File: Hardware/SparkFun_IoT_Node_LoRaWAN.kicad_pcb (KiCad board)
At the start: 4 copper layers, 59 x 82 mm, 234 parts, among them J1 USB_C_Receptacle, J10 microSD_Friction, J11 Qwiic_RA, J2 Conn_01x03, J3 USB_C_Receptacle, J4 SWD, J5 Conn_01x10, J6 Conn_01x10, J7 Conn_01x10, J8 Conn_01x10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

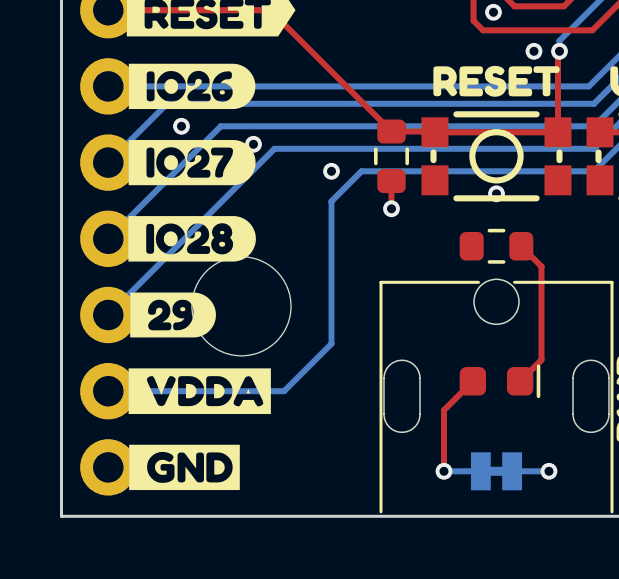
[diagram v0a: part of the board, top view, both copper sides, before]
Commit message: Cosmetic tweaks
Nudge IO 29 silk away from mounting hole
Add VDDA RC filter cutoff frequency
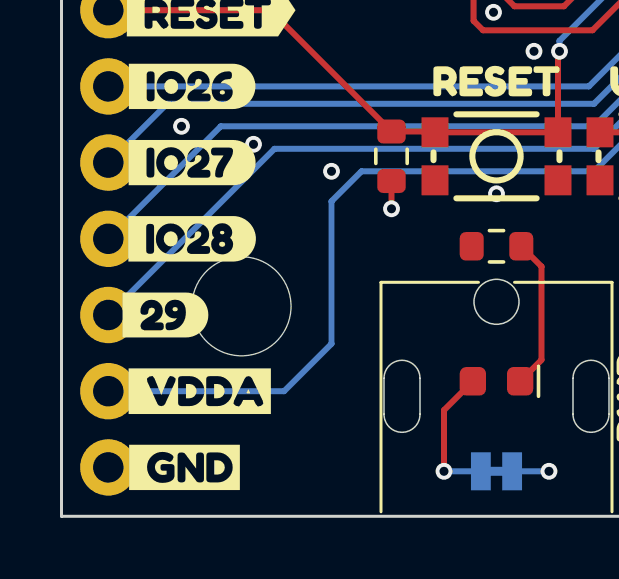
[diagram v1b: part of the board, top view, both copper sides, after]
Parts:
- moved kibuzzard-669EA5FC 0.25 mm to (74.0, 134.3)
- moved kibuzzard-669EA604 0.25 mm to (74.0, 134.3)
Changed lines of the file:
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@@
 	(footprint "kibuzzard-669EA604"
 		(layer "F.Cu")
-		(at 74.219 134.29)
+		(at 73.965 134.29)
 		(descr "Generated with KiBuzzard")
 		(tags "kb_params=eyJBbGlnbm1lbnRDaG9pY2UiOiAiQ2VudGVyIiwgIkNhcExlZnRDaG9pY2UiOiAiWyIsICJDYXBSaWdodENob2ljZSI6ICIpIiwgIkZvbnRDb21ib0JveCI6ICJGcmVkZHlTcGFyay1SZWd1bGFyIiwgIkhlaWdodEN0cmwiOiAxLjAsICJMYXllckNvbWJvQm94IjogIkYuU2lsa1MiLCAiTGluZVNwYWNpbmdDdHJsIjogMS41LCAiTXVsdGlMaW5lVGV4dCI6ICIyOSIsICJQYWRkaW5nQm90dG9tQ3RybCI6IDIuMCwgIlBhZGRpbmdMZWZ0Q3RybCI6IDUuMCwgIlBhZGRpbmdSaWdodEN0cmwiOiAwLjAsICJQYWRkaW5nVG9wQ3RybCI6IDIuMCwgIldpZHRoQ3RybCI6IDAuMCwgImFkdmFuY2VkQ2hlY2tib3giOiBmYWxzZSwgImlubGluZUZvcm1hdFRleHRib3giOiBmYWxzZSwgImxpbmVvdmVyU3R5bGVDaG9pY2UiOiAiU3F1YXJlIiwgImxpbmVvdmVyVGhpY2tuZXNzQ3RybCI6IDF9")
@@
 	(footprint "kibuzzard-669EA5FC"
 		(layer "B.Cu")
-		(at 74.219 134.29 180)
+		(at 73.965 134.29 180)
 		(descr "Generated with KiBuzzard")
 		(tags "kb_params=eyJBbGlnbm1lbnRDaG9pY2UiOiAiQ2VudGVyIiwgIkNhcExlZnRDaG9pY2UiOiAiKCIsICJDYXBSaWdodENob2ljZSI6ICJdIiwgIkZvbnRDb21ib0JveCI6ICJGcmVkZHlTcGFyay1SZWd1bGFyIiwgIkhlaWdodEN0cmwiOiAxLjAsICJMYXllckNvbWJvQm94IjogIkYuU2lsa1MiLCAiTGluZVNwYWNpbmdDdHJsIjogMS41LCAiTXVsdGlMaW5lVGV4dCI6ICIyOSIsICJQYWRkaW5nQm90dG9tQ3RybCI6IDIuMCwgIlBhZGRpbmdMZWZ0Q3RybCI6IDAuMCwgIlBhZGRpbmdSaWdodEN0cmwiOiA1LjAsICJQYWRkaW5nVG9wQ3RybCI6IDIuMCwgIldpZHRoQ3RybCI6IDAuMCwgImFkdmFuY2VkQ2hlY2tib3giOiBmYWxzZSwgImlubGluZUZvcm1hdFRleHRib3giOiBmYWxzZSwgImxpbmVvdmVyU3R5bGVDaG9pY2UiOiAiU3F1YXJlIiwgImxpbmVvdmVyVGhpY2tuZXNzQ3RybCI6IDF9")

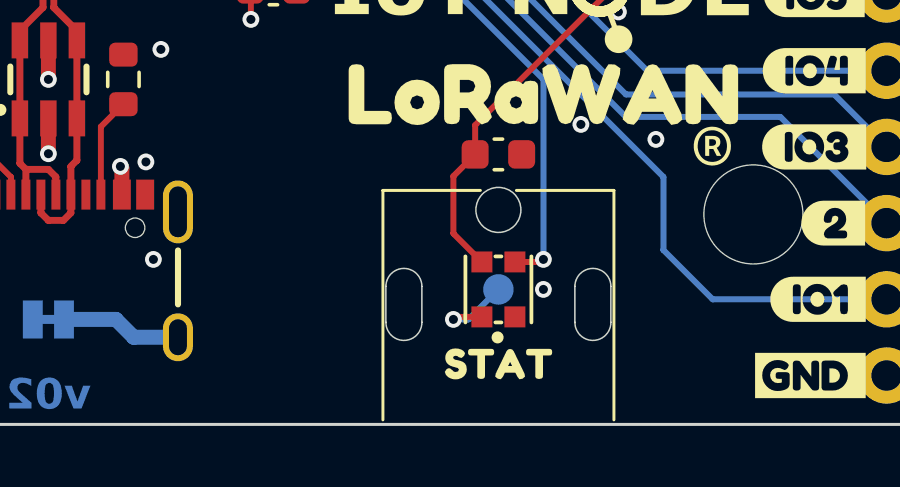
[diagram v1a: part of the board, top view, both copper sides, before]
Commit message: Move STAT silk
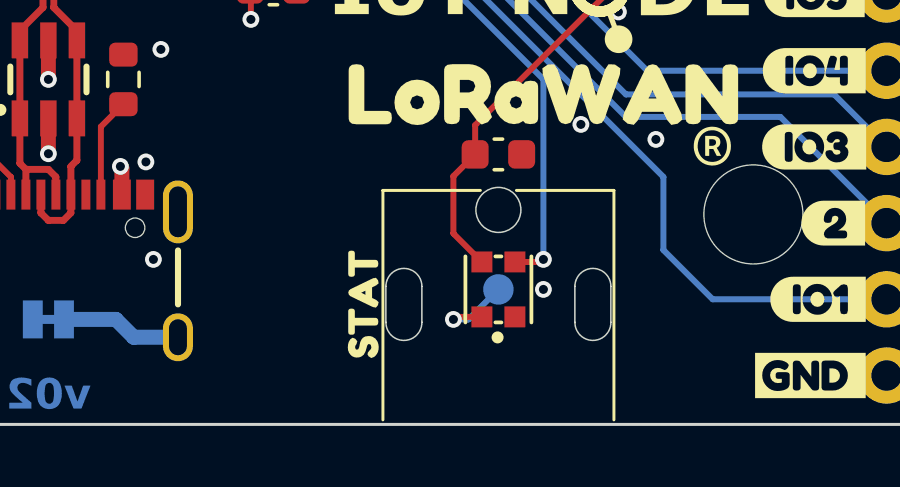
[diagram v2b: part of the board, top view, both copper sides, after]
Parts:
- moved kibuzzard-66999523 4.92 mm to (110.5, 137.0), turned to 90 degrees
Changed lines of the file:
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@@
 	(footprint "kibuzzard-66999523"
 		(layer "F.Cu")
-		(at 115 138.9875)
+		(at 110.5 137 90)
 		(descr "Generated with KiBuzzard")
 		(tags "kb_params=eyJBbGlnbm1lbnRDaG9pY2UiOiAiQ2VudGVyIiwgIkNhcExlZnRDaG9pY2UiOiAiIiwgIkNhcFJpZ2h0Q2hvaWNlIjogIiIsICJGb250Q29tYm9Cb3giOiAiRnJlZGR5U3BhcmstUmVndWxhciIsICJIZWlnaHRDdHJsIjogMS4wLCAiTGF5ZXJDb21ib0JveCI6ICJGLlNpbGtTIiwgIkxpbmVTcGFjaW5nQ3RybCI6IDEuNSwgIk11bHRpTGluZVRleHQiOiAiU1RBVCIsICJQYWRkaW5nQm90dG9tQ3RybCI6IDIuMCwgIlBhZGRpbmdMZWZ0Q3RybCI6IDAuMCwgIlBhZGRpbmdSaWdodEN0cmwiOiAwLjAsICJQYWRkaW5nVG9wQ3RybCI6IDIuMCwgIldpZHRoQ3RybCI6IDAuMCwgImFkdmFuY2VkQ2hlY2tib3giOiBmYWxzZSwgImlubGluZUZvcm1hdFRleHRib3giOiBmYWxzZSwgImxpbmVvdmVyU3R5bGVDaG9pY2UiOiAiU3F1YXJlIiwgImxpbmVvdmVyVGhpY2tuZXNzQ3RybCI6IDF9")
 		(property "Reference" "kibuzzard-66999523"
-			(at 0 -3.568029 0)
+			(at 0 -3.568029 90)
 			(layer "F.SilkS")
 			(hide yes)
@@
 		)
 		(property "Value" "G***"
-			(at 0 3.568029 0)
+			(at 0 3.568029 90)
 			(layer "F.SilkS")
 			(hide yes)
@@
 		)
 		(property "Footprint" ""
-			(at 0 0 0)
+			(at 0 0 90)
 			(layer "F.Fab")
 			(hide yes)
@@
 		)
 		(property "Datasheet" ""
-			(at 0 0 0)
+			(at 0 0 90)
 			(layer "F.Fab")
 			(hide yes)
@@
 		)
 		(property "Description" ""
-			(at 0 0 0)
+			(at 0 0 90)
 			(layer "F.Fab")
 			(hide yes)
@@
 		(fp_poly
 			(pts
+				(xy 1.684549 -0.505722) (xy 1.725322 -0.503577) (xy 1.757511 -0.492132) (xy 1.784692 -0.458512)
+				(xy 1.793276 -0.395565) (xy 1.784692 -0.332618) (xy 1.756795 -0.298999) (xy 1.723891 -0.287554)
+				(xy 1.683119 -0.285408) (xy 1.485694 -0.285408) (xy 1.485694 0.369814) (xy 1.483548 0.41774) (xy 1.469957 0.455651)
+				(xy 1.4299 0.487124) (xy 1.355508 0.497139) (xy 1.281831 0.487124) (xy 1.243205 0.454936) (xy 1.230329 0.416309)
+				(xy 1.228183 0.368383) (xy 1.228183 -0.285408) (xy 1.029328 -0.285408) (xy 0.988555 -0.287554) (xy 0.956366 -0.298999)
+				(xy 0.929185 -0.332618) (xy 0.920601 -0.396996) (xy 0.929185 -0.459227) (xy 0.957082 -0.492132)
+				(xy 0.989986 -0.503577) (xy 1.030758 -0.505722) (xy 1.684549 -0.505722)
+			)
+			(stroke
+				(width 0)
+				(type solid)
+			)
+			(fill solid)
+			(layer "F.SilkS")
+		)
+		(fp_poly
+			(pts
 				(xy -0.248212 -0.505722) (xy -0.207439 -0.503577) (xy -0.17525 -0.492132) (xy -0.148069 -0.458512)
 				(xy -0.139485 -0.395565) (xy -0.148069 -0.332618) (xy -0.175966 -0.298999) (xy -0.20887 -0.287554)
@@
 			)
 			(stroke
-				(width 0)
-				(type solid)
-			)
-			(fill solid)
-			(layer "F.SilkS")
-		)
-		(fp_poly
-			(pts
-				(xy 1.684549 -0.505722) (xy 1.725322 -0.503577) (xy 1.757511 -0.492132) (xy 1.784692 -0.458512)
-				(xy 1.793276 -0.395565) (xy 1.784692 -0.332618) (xy 1.756795 -0.298999) (xy 1.723891 -0.287554)
-				(xy 1.683119 -0.285408) (xy 1.485694 -0.285408) (xy 1.485694 0.369814) (xy 1.483548 0.41774) (xy 1.469957 0.455651)
-				(xy 1.4299 0.487124) (xy 1.355508 0.497139) (xy 1.281831 0.487124) (xy 1.243205 0.454936) (xy 1.230329 0.416309)
-				(xy 1.228183 0.368383) (xy 1.228183 -0.285408) (xy 1.029328 -0.285408) (xy 0.988555 -0.287554) (xy 0.956366 -0.298999)
-				(xy 0.929185 -0.332618) (xy 0.920601 -0.396996) (xy 0.929185 -0.459227) (xy 0.957082 -0.492132)
-				(xy 0.989986 -0.503577) (xy 1.030758 -0.505722) (xy 1.684549 -0.505722)
-			)
-			(stroke

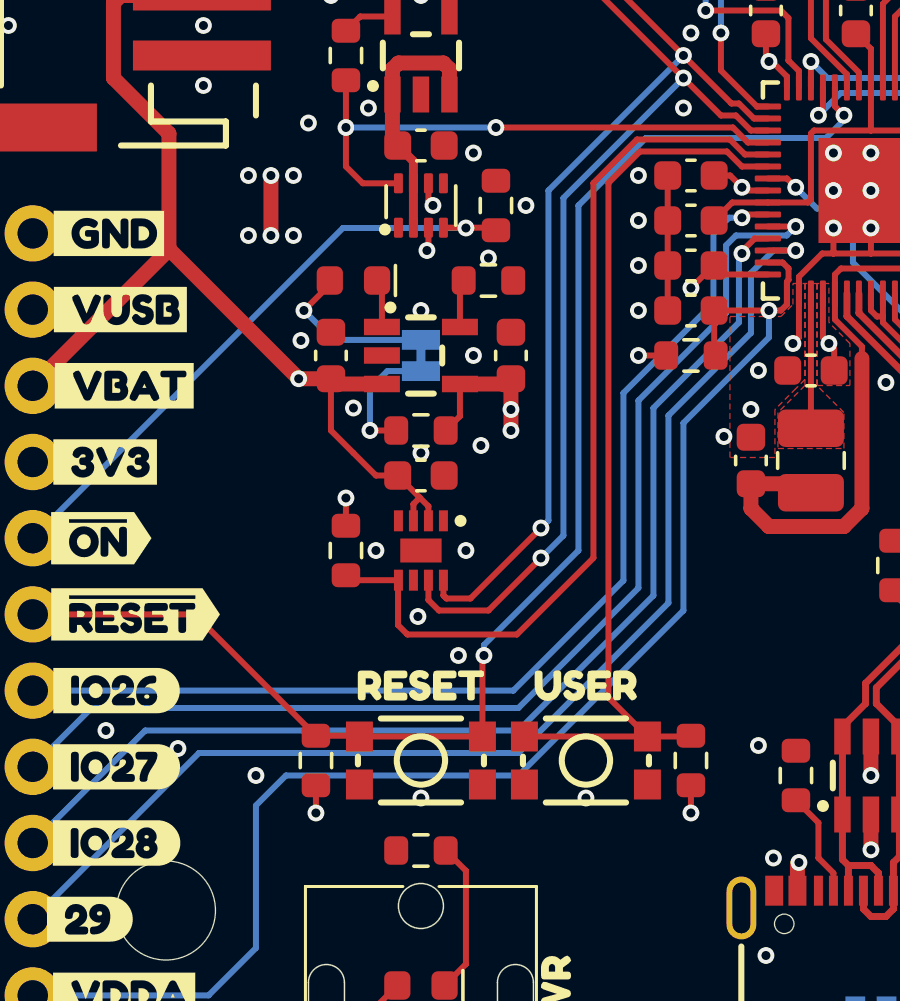
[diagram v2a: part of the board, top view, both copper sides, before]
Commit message: Spread out reset and user buttons
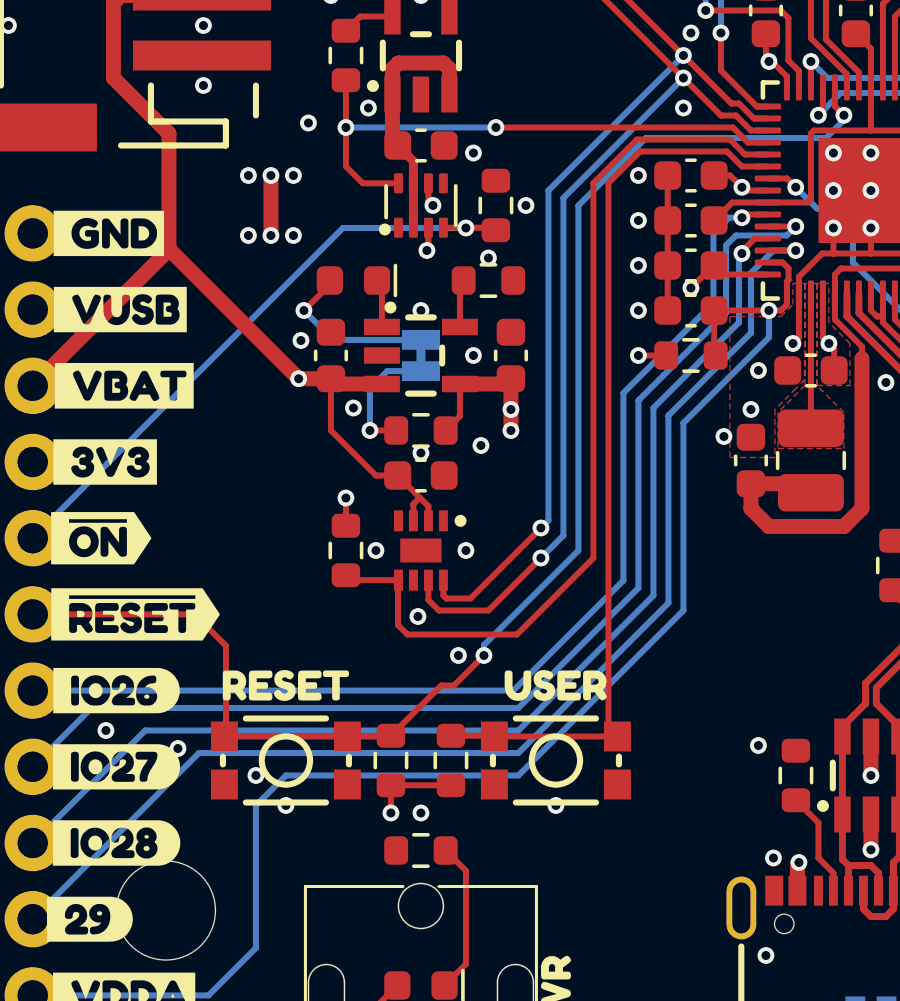
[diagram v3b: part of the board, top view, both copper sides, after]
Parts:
- moved R22 8.00 mm to (86.0, 129.0)
- moved SW3 4.50 mm to (80.5, 129.0)
- moved kibuzzard-6691B8DD 4.50 mm to (80.5, 126.5)
- moved R25 2.50 mm to (84.0, 129.0)
- moved SW2 1.00 mm to (89.5, 129.0)
- moved kibuzzard-669A9B0A 1.00 mm to (89.5, 126.5)
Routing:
- net 3.3V: track 59.5 -> 60.5 mm, vias 24 -> 23
- net GND: vias 167 -> 168
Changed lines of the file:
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@@
 	(footprint "SparkFun-Switch:Push_SMD_4.6x2.8mm"
 		(layer "F.Cu")
-		(at 90.5 129 180)
+		(at 89.5 129 180)
 		(tags "SparkFun Momentary Switch (Pushbutton)")
 		(property "Reference" "SW2"
@@
 	(footprint "SparkFun-Resistor:R_0603_1608Metric"
 		(layer "F.Cu")
-		(at 94 129 90)
+		(at 86 129 90)
 		(descr "Resistor SMD 0603 (1608 Metric), square (rectangular) end terminal, IPC_7351 nominal, (Body size source: IPC-SM-782 page 72, https://www.pcb-3d.com/wordpress/wp-content/uploads/ipc-sm-782a_amendment_1_and_2.pdf), generated with kicad-footprint-generator")
 		(tags "SparkFun resistor")
@@
 	(footprint "SparkFun-Switch:Push_SMD_4.6x2.8mm"
 		(layer "F.Cu")
-		(at 85 129 180)
+		(at 80.5 129 180)
 		(tags "SparkFun Momentary Switch (Pushbutton)")
 		(property "Reference" "SW3"
@@
 	(footprint "kibuzzard-6691B8DD"
 		(layer "F.Cu")
-		(at 85 126.5)
+		(at 80.5 126.5)
 		(descr "Generated with KiBuzzard")
 		(tags "kb_params=eyJBbGlnbm1lbnRDaG9pY2UiOiAiQ2VudGVyIiwgIkNhcExlZnRDaG9pY2UiOiAiIiwgIkNhcFJpZ2h0Q2hvaWNlIjogIiIsICJGb250Q29tYm9Cb3giOiAiRnJlZGR5U3BhcmstUmVndWxhciIsICJIZWlnaHRDdHJsIjogMS4wLCAiTGF5ZXJDb21ib0JveCI6ICJGLlNpbGtTIiwgIkxpbmVTcGFjaW5nQ3RybCI6IDEuNSwgIk11bHRpTGluZVRleHQiOiAiUkVTRVQiLCAiUGFkZGluZ0JvdHRvbUN0cmwiOiAyLjAsICJQYWRkaW5nTGVmdEN0cmwiOiAwLjAsICJQYWRkaW5nUmlnaHRDdHJsIjogMC4wLCAiUGFkZGluZ1RvcEN0cmwiOiAyLjAsICJXaWR0aEN0cmwiOiAwLjAsICJhZHZhbmNlZENoZWNrYm94IjogZmFsc2UsICJpbmxpbmVGb3JtYXRUZXh0Ym94IjogZmFsc2UsICJsaW5lb3ZlclN0eWxlQ2hvaWNlIjogIlNxdWFyZSIsICJsaW5lb3ZlclRoaWNrbmVzc0N0cmwiOiAxfQ==")
@@
 	(footprint "kibuzzard-669A9B0A"
 		(layer "F.Cu")
-		(at 90.5 126.5)
+		(at 89.5 126.5)
 		(descr "Generated with KiBuzzard")
 		(tags "kb_params=eyJBbGlnbm1lbnRDaG9pY2UiOiAiQ2VudGVyIiwgIkNhcExlZnRDaG9pY2UiOiAiIiwgIkNhcFJpZ2h0Q2hvaWNlIjogIiIsICJGb250Q29tYm9Cb3giOiAiRnJlZGR5U3BhcmstUmVndWxhciIsICJIZWlnaHRDdHJsIjogMS4wLCAiTGF5ZXJDb21ib0JveCI6ICJGLlNpbGtTIiwgIkxpbmVTcGFjaW5nQ3RybCI6IDEuNSwgIk11bHRpTGluZVRleHQiOiAiVVNFUiIsICJQYWRkaW5nQm90dG9tQ3RybCI6IDIuMCwgIlBhZGRpbmdMZWZ0Q3RybCI6IDAuMCwgIlBhZGRpbmdSaWdodEN0cmwiOiAwLjAsICJQYWRkaW5nVG9wQ3RybCI6IDIuMCwgIldpZHRoQ3RybCI6IDAuMCwgImFkdmFuY2VkQ2hlY2tib3giOiBmYWxzZSwgImlubGluZUZvcm1hdFRleHRib3giOiBmYWxzZSwgImxpbmVvdmVyU3R5bGVDaG9pY2UiOiAiU3F1YXJlIiwgImxpbmVvdmVyVGhpY2tuZXNzQ3RybCI6IDF9")
@@
 	(footprint "SparkFun-Resistor:R_0603_1608Metric"
 		(layer "F.Cu")
-		(at 81.5 129 90)
+		(at 84 129 90)
 		(descr "Resistor SMD 0603 (1608 Metric), square (rectangular) end terminal, IPC_7351 nominal, (Body size source: IPC-SM-782 page 72, https://www.pcb-3d.com/wordpress/wp-content/uploads/ipc-sm-782a_amendment_1_and_2.pdf), generated with kicad-footprint-generator")
 		(tags "SparkFun resistor")
@@
 		(layer "Dwgs.User")
 		(pts
-			(xy 85 129) (xy 100 129)
-		)
-		(height 21)
-		(gr_text "15 mm"
-			(at 92.5 148.85 0)
-			(layer "Dwgs.User")
-			(effects
-				(font
-					(size 1 1)
-					(thickness 0.15)
-				)
-			)
-		)
-		(format
-			(prefix "")
-			(suffix "")
-			(units 3)
-			(units_format 1)
-			(precision 4) suppress_zeroes)
-		(style
-			(thickness 0.15)
-			(arrow_length 1.27)
-			(text_position_mode 0)
-			(extension_height 0.58642)
-			(extension_offset 0.5) keep_text_aligned)
-	)
-	(dimension
-		(type aligned)
-		(layer "Dwgs.User")
-		(pts
 			(xy 58.5 81) (xy 141.5 81)
 		)
@@
 		(layer "Dwgs.User")
 		(pts
+			(xy 80.5 129) (xy 100 129)
+		)
+		(height 21)
+		(gr_text "19.5 mm"
+			(at 90.25 148.85 0)
+			(layer "Dwgs.User")
+			(effects
+				(font
+					(size 1 1)
+					(thickness 0.15)
+				)
+			)
+		)
+		(format
+			(prefix "")
+			(suffix "")
+			(units 3)
+			(units_format 1)
+			(precision 4) suppress_zeroes)
+		(style
+			(thickness 0.15)
+			(arrow_length 1.27)
+			(text_position_mode 0)
+			(extension_height 0.58642)
+			(extension_offset 0.5) keep_text_aligned)
+	)
+	(dimension
+		(type aligned)
+		(layer "Dwgs.User")
+		(pts
 			(xy 127.94 60.63) (xy 127.94 100)
 		)
@@
 		(layer "Dwgs.User")
 		(pts
-			(xy 90.5 129) (xy 100 129)
+			(xy 89.5 129) (xy 100 129)
 		)
 		(height 18)
-		(gr_text "9.5 mm"
-			(at 95.25 145.85 0)
+		(gr_text "10.5 mm"
+			(at 94.75 145.85 0)
 			(layer "Dwgs.User")
 			(effects
@@
 	)
 	(via
-		(at 90.5 130.25)
+		(at 89.5 130.5)
 		(size 0.56)
 		(drill 0.3)
@@
 	)
 	(via
-		(at 85 130.25)
+		(at 85 130.75)
 		(size 0.56)
 		(drill 0.3)
@@
 	)
 	(via
+		(at 80.5 130.5)
+		(size 0.56)
+		(drill 0.3)
+		(layers "F.Cu" "B.Cu")
+		(net 2)
+	)
+	(via
 		(at 82.75 101.75)
 		(size 0.56)
@@
 	)
 	(segment
-		(start 94 129.825)
-		(end 94 130.75)
+		(start 84 129.825)
+		(end 84 130.75)
 		(width 0.2)
 		(layer "F.Cu")
@@
 	)
 	(segment
+		(start 84 129.825)
+		(end 86 129.825)
+		(width 0.2)
+		(layer "F.Cu")
+		(net 4)
+	)
+	(segment
 		(start 100.2 114.2)
 		(end 100.4 114.2)
@@
 		(net 4)
 	)
-	(segment
-		(start 81.5 129.825)
-		(end 81.5 130.75)
-		(width 0.2)
-		(layer "F.Cu")
-		(net 4)
-	)
 	(via
 		(at 106.75 127.5)
@@
 	)
 	(via
-		(at 94 130.75)
+		(at 84 130.75)
 		(size 0.56)
 		(drill 0.3)
@@
 	)
 	(via
-		(at 81.5 130.75)
-		(size 0.56)
-		(drill 0.3)
-		(layers "F.Cu" "B.Cu")
-		(net 4)
-	)
-	(via
 		(at 114.25 112.5)
 		(size 0.56)
@@
 	)
 	(segment
-		(start 87.1 125.5)
-		(end 87.05 125.55)
+		(start 83.975 128.2)
+		(end 84 128.175)
 		(width 0.2)
 		(layer "F.Cu")
@@
 	)
 	(segment
-		(start 87.05 128.2)
-		(end 82.95 128.2)
+		(start 77.455 124.13)
+		(end 78.5 125.175)
 		(width 0.2)
 		(layer "F.Cu")
@@
 	)
 	(segment
-		(start 82.925 128.175)
-		(end 82.95 128.2)
+		(start 84 128.175)
+		(end 85.675 126.5)
 		(width 0.2)
 		(layer "F.Cu")
@@
 	)
 	(segment
-		(start 87.05 125.55)
-		(end 87.05 128.2)
+		(start 99.1 107.493)
+		(end 98.8 107.193)
 		(width 0.2)
 		(layer "F.Cu")
@@
 	)
 	(segment
-		(start 99.1 107.493)
-		(end 98.8 107.193)
+		(start 72.06 124.13)
+		(end 77.455 124.13)
 		(width 0.2)
 		(layer "F.Cu")
@@
 	)
 	(segment
-		(start 81.5 128.175)
-		(end 82.925 128.175)
+		(start 86.1 126.5)
+		(end 87.1 125.5)
 		(width 0.2)
 		(layer "F.Cu")
@@
 	)
 	(segment
-		(start 72.06 124.13)
-		(end 77.455 124.13)
+		(start 78.45 128.2)
+		(end 82.55 128.2)
 		(width 0.2)
 		(layer "F.Cu")
@@
 	)
 	(segment
-		(start 98.8 107.193)
-		(end 98.8 106.5635)
+		(start 85.675 126.5)
+		(end 86.1 126.5)
 		(width 0.2)
 		(layer "F.Cu")
@@
 	)
 	(segment
-		(start 77.455 124.13)
-		(end 81.5 128.175)
+		(start 78.5 125.175)
+		(end 78.5 128.175)
+		(width 0.2)
+		(layer "F.Cu")
+		(net 28)
+	)
+	(segment
+		(start 82.55 128.2)
+		(end 83.975 128.2)
+		(width 0.2)
+		(layer "F.Cu")
+		(net 28)
+	)
+	(segment
+		(start 98.8 107.193)
+		(end 98.8 106.5635)
 		(width 0.2)
 		(layer "F.Cu")
@@
 	)
 	(segment
-		(start 92.55 128.2)
-		(end 91.25 126.9)
+		(start 86 128.175)
+		(end 87.425 128.175)
 		(width 0.2)
 		(layer "F.Cu")
@@
 	)
 	(segment
-		(start 91.25 126.9)
-		(end 91.25 109.75)
+		(start 91.55 128.2)
+		(end 87.45 128.2)
 		(width 0.2)
 		(layer "F.Cu")
@@
 	)
 	(segment
-		(start 92.55 128.2)
-		(end 88.45 128.2)
+		(start 92.3 108.7)
+		(end 95.2 108.7)
 		(width 0.2)
 		(layer "F.Cu")
@@
 	)
 	(segment
-		(start 95.2 108.7)
-		(end 95.7 109.2)
+		(start 91.55 128.2)
+		(end 91.25 127.9)
 		(width 0.2)
 		(layer "F.Cu")
@@
 	)
 	(segment
-		(start 91.25 109.75)
-		(end 92.3 108.7)
+		(start 95.7 109.2)
+		(end 96.5635 109.2)
 		(width 0.2)
 		(layer "F.Cu")
@@
 	)
 	(segment
-		(start 95.7 109.2)
-		(end 96.5635 109.2)
+		(start 87.425 128.175)
+		(end 87.45 128.2)
 		(width 0.2)
 		(layer "F.Cu")
@@
 	)
 	(segment
-		(start 92.3 108.7)
-		(end 95.2 108.7)
+		(start 91.25 109.75)
+		(end 92.3 108.7)
 		(width 0.2)
 		(layer "F.Cu")
@@
 	)
 	(segment
-		(start 93.975 128.2)
-		(end 94 128.175)
+		(start 95.2 108.7)
+		(end 95.7 109.2)
 		(width 0.2)
 		(layer "F.Cu")
@@
 	)
 	(segment
-		(start 92.55 128.2)
-		(end 93.975 128.2)
+		(start 91.25 127.9)
+		(end 91.25 109.75)
 		(width 0.2)
 		(layer "F.Cu")

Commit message: Add soldermask cutout for CBI footprints
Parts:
- ST1, ST2, ST3, ST4: value Standoff -> STAND-OFF
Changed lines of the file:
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@@
 			)
 		)
-		(property "Value" "Standoff"
+		(property "Value" "STAND-OFF"
 			(at 0 2.032 0)
 			(layer "F.Fab")
@@
 		)
 		(fp_line
+			(start -0.1 3.15)
+			(end 1.1 3.15)
+			(stroke
+				(width 1.25)
+				(type default)
+			)
+			(layer "F.Mask")
+		)
+		(fp_line
+			(start -0.1 -3.15)
+			(end 1.1 -3.15)
+			(stroke
+				(width 1.25)
+				(type default)
+			)
+			(layer "F.Mask")
+		)
+		(fp_circle
+			(center -2.65 0)
+			(end -2.275 0)
+			(stroke
+				(width 0.8)
+				(type default)
+			)
+			(fill none)
+			(layer "F.Mask")
+		)
+		(fp_line
 			(start 1.1 3.75)
 			(end -0.1 3.75)
@@
 		)
 		(fp_line
+			(start -0.1 3.15)
+			(end 1.1 3.15)
+			(stroke
+				(width 1.25)
+				(type default)
+			)
+			(layer "F.Mask")
+		)
+		(fp_line
+			(start -0.1 -3.15)
+			(end 1.1 -3.15)
+			(stroke
+				(width 1.25)
+				(type default)
+			)
+			(layer "F.Mask")
+		)
+		(fp_circle
+			(center -2.65 0)
+			(end -2.275 0)
+			(stroke
+				(width 0.8)
+				(type default)
+			)
+			(fill none)
+			(layer "F.Mask")
+		)
+		(fp_line
 			(start 1.1 3.75)
 			(end -0.1 3.75)
@@
 			)
 		)
-		(property "Value" "Standoff"
+		(property "Value" "STAND-OFF"
 			(at 0 2.032 0)
 			(layer "F.Fab")
@@
 			)
 		)
-		(property "Value" "Standoff"
+		(property "Value" "STAND-OFF"
 			(at 0 2.032 0)
 			(layer "F.Fab")
@@
 			)
 		)
-		(property "Value" "Standoff"
+		(property "Value" "STAND-OFF"
 			(at 0 2.032 0)
 			(layer "F.Fab")
